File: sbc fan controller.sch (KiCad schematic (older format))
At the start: 26 parts, among them J1 Conn_01x13, J10 ISP-6, J2 Conn_01x02, J3 TEST_1P, J4 Conn_01x04, J5 Conn_01x04, J6 Conn_01x03, J7 TEST_1P, J8 TEST_2P, J9 Conn_Coaxial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

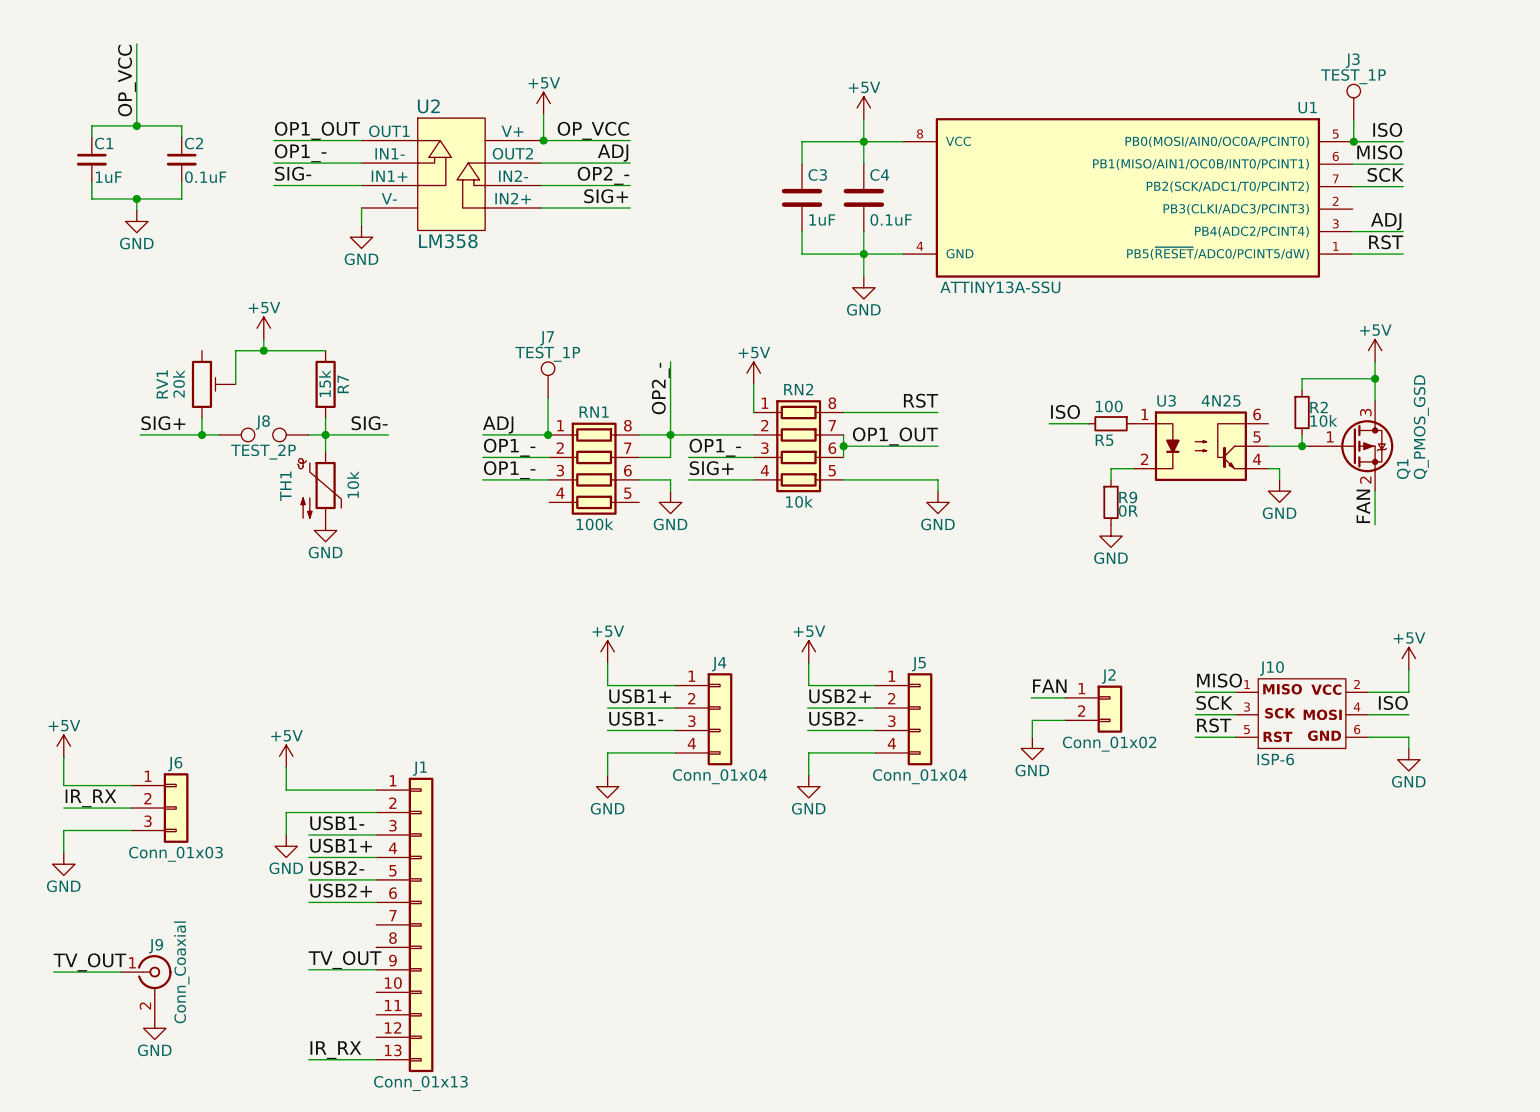
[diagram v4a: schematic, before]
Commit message: Simplified design, dropped amp; added isolated ground
After testing the dual amp circuit against a simple voltage divider, ADC yields enough resolution to discern heat levels in order to accommodate a look up table for fan speed. Isolated ground plane for switching area included to minimize EMF impact on integrated wifi.
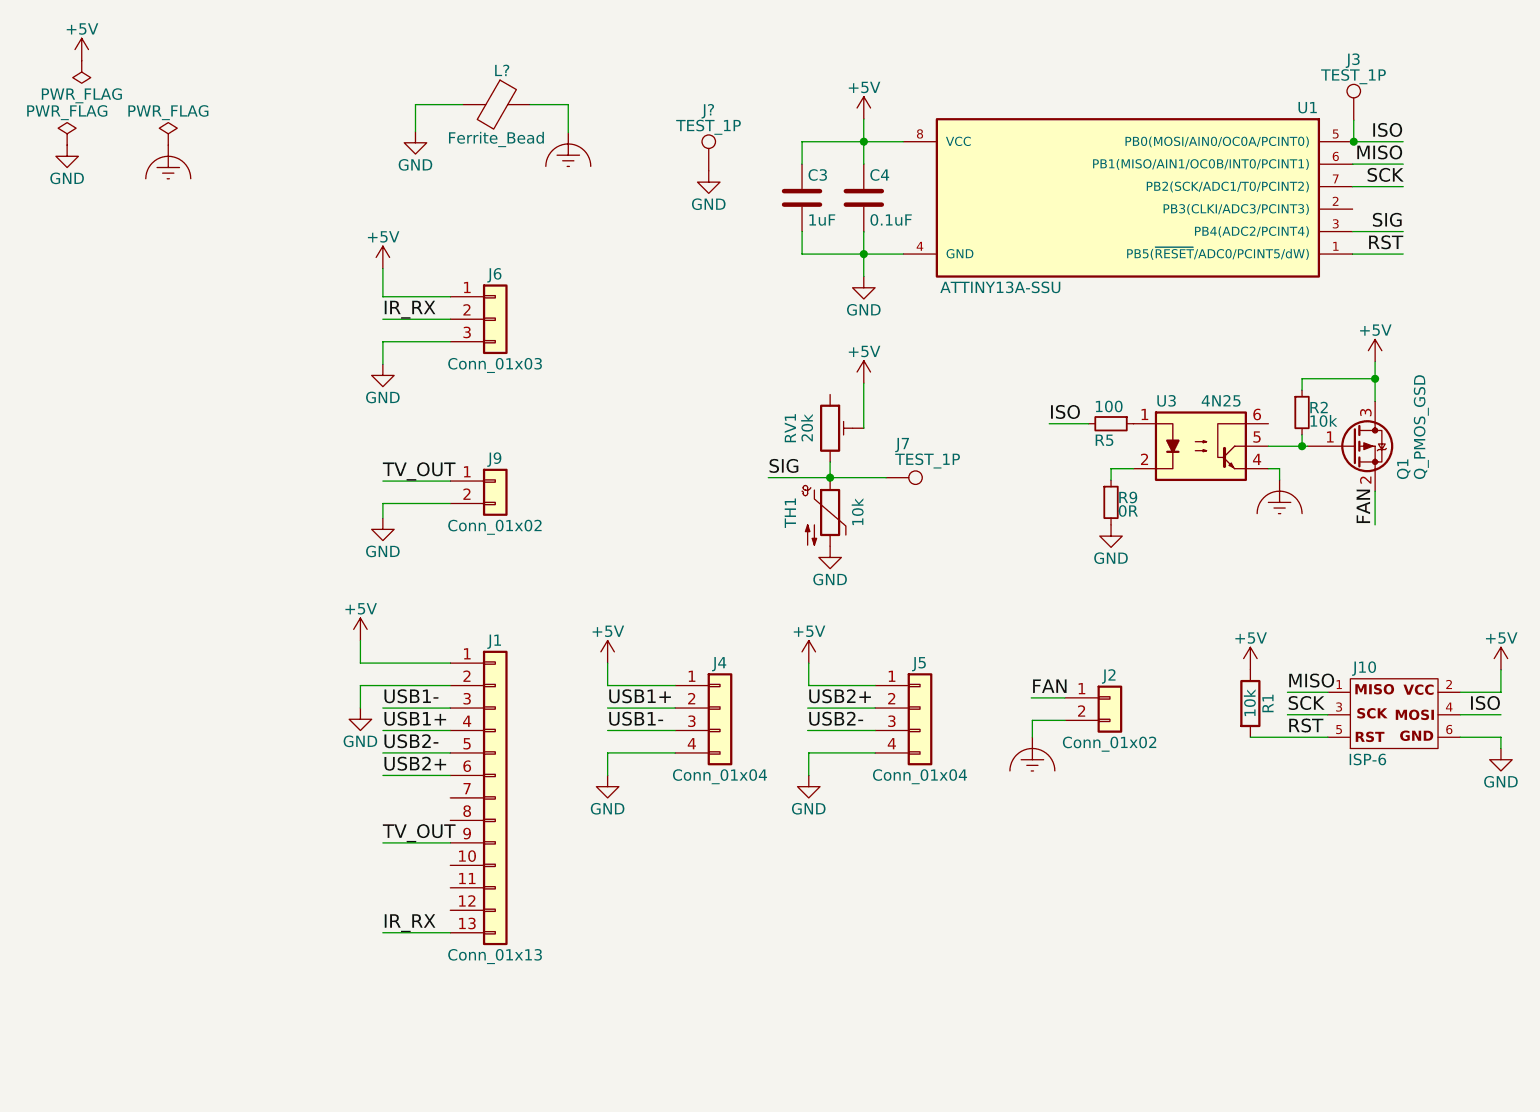
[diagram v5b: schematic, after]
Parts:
- removed C1: 1uF, Capacitors_SMD:C_0603, symbol C_Small
- removed C2: 0.1uF, Capacitors_SMD:C_0603, symbol C_Small
- removed J8: TEST_2P, node_nrf:Measurement_Point_Round-SMD-2-Pad_Small, symbol TEST_2P
- removed J9: Conn_Coaxial, rca:RCA1, symbol Conn_Coaxial
- removed R7: 15k, Resistors_SMD:R_0805, symbol R
- removed RN1: 100k, node_nrf:YC164J, symbol R_Pack04
- removed RN2: 10k, node_nrf:YC164J, symbol R_Pack04
- removed U2: LM358, Housings_SOIC:SOIC-8_3.9x4.9mm_Pitch1.27mm, symbol TL972
- added J9: Conn_01x02, Connectors_JST:JST_ZE_S02B-ZESK-2D_02x1.5mm_Angled, symbol Conn_01x02
- added J?: TEST_1P, symbol TEST_1P
- added L?: Ferrite_Bead, symbol Ferrite_Bead
- added R1: 10k, Resistors_SMD:R_0805, symbol R
- J4: footprint Connectors_JST:JST_SH_BM04B-SRSS-TB_04x1.00mm_Straight -> Connectors_JST:JST_ZE_S04B-ZESK-2D_04x1.5mm_Angled
- J5: footprint Connectors_JST:JST_SH_BM04B-SRSS-TB_04x1.00mm_Straight -> Connectors_JST:JST_ZE_SM04B-ZESS-TB_04x1.5mm_Angled
- J6: footprint Connectors_JST:JST_SH_BM03B-SRSS-TB_03x1.00mm_Straight -> Connectors_JST:JST_ZE_SM03B-ZESS-TB_03x1.5mm_Angled
- TH1: footprint Resistors_THT:R_Axial_DIN0204_L3.6mm_D1.6mm_P2.54mm_Vertical -> Connectors_JST:JST_ZE_SM02B-ZESS-TB_02x1.5mm_Angled
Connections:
- net ADJ is gone; now on net SIG: J7.1, U1.3 (PB4(ADC2/PCINT4))
- net SIG+ is gone; now on net SIG: RV1.3
- net +5V: now also R1.1
- net GND: now also J9.2 (Pin_2), J?.1, L?.2; no longer J2.2 (Pin_2), U3.4
- net RST: now also R1.2
- net TV_OUT: now also J9.1 (Pin_1)
- net SIG: now reaches TH1.1
- new net Earth_Clean: J2.2 (Pin_2), L?.1, U3.4
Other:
- moved on the sheet: J1, J10, J6, RV1, TH1

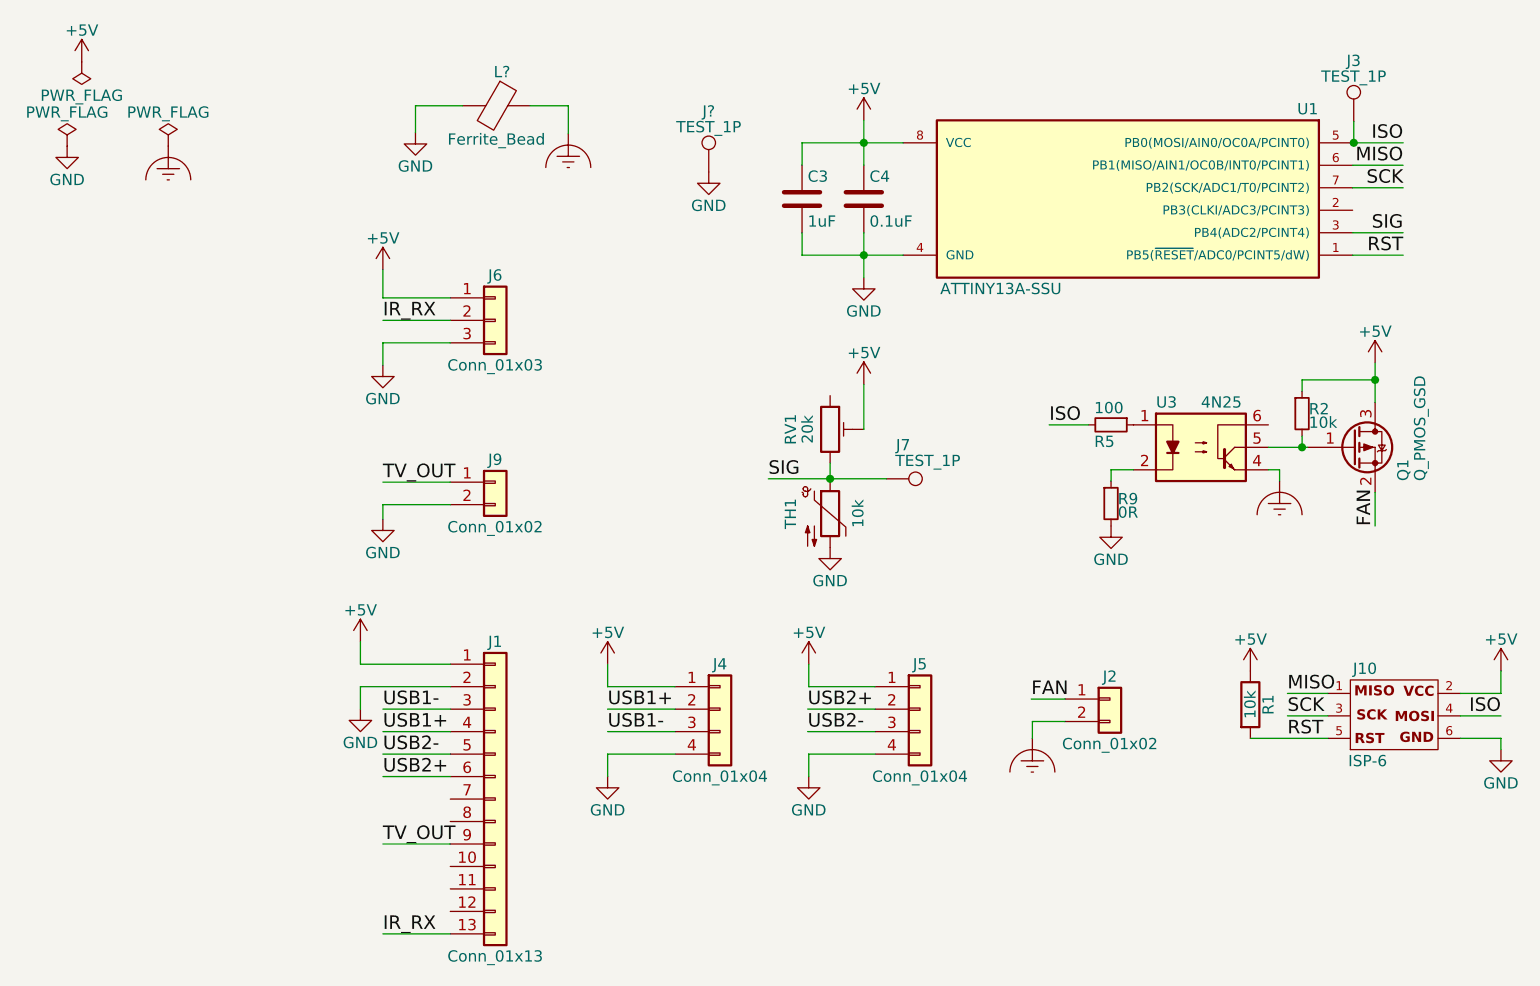
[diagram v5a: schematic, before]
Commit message: Final layout
Simplified layout and tested each footprint with a hard copy layout actual parts.
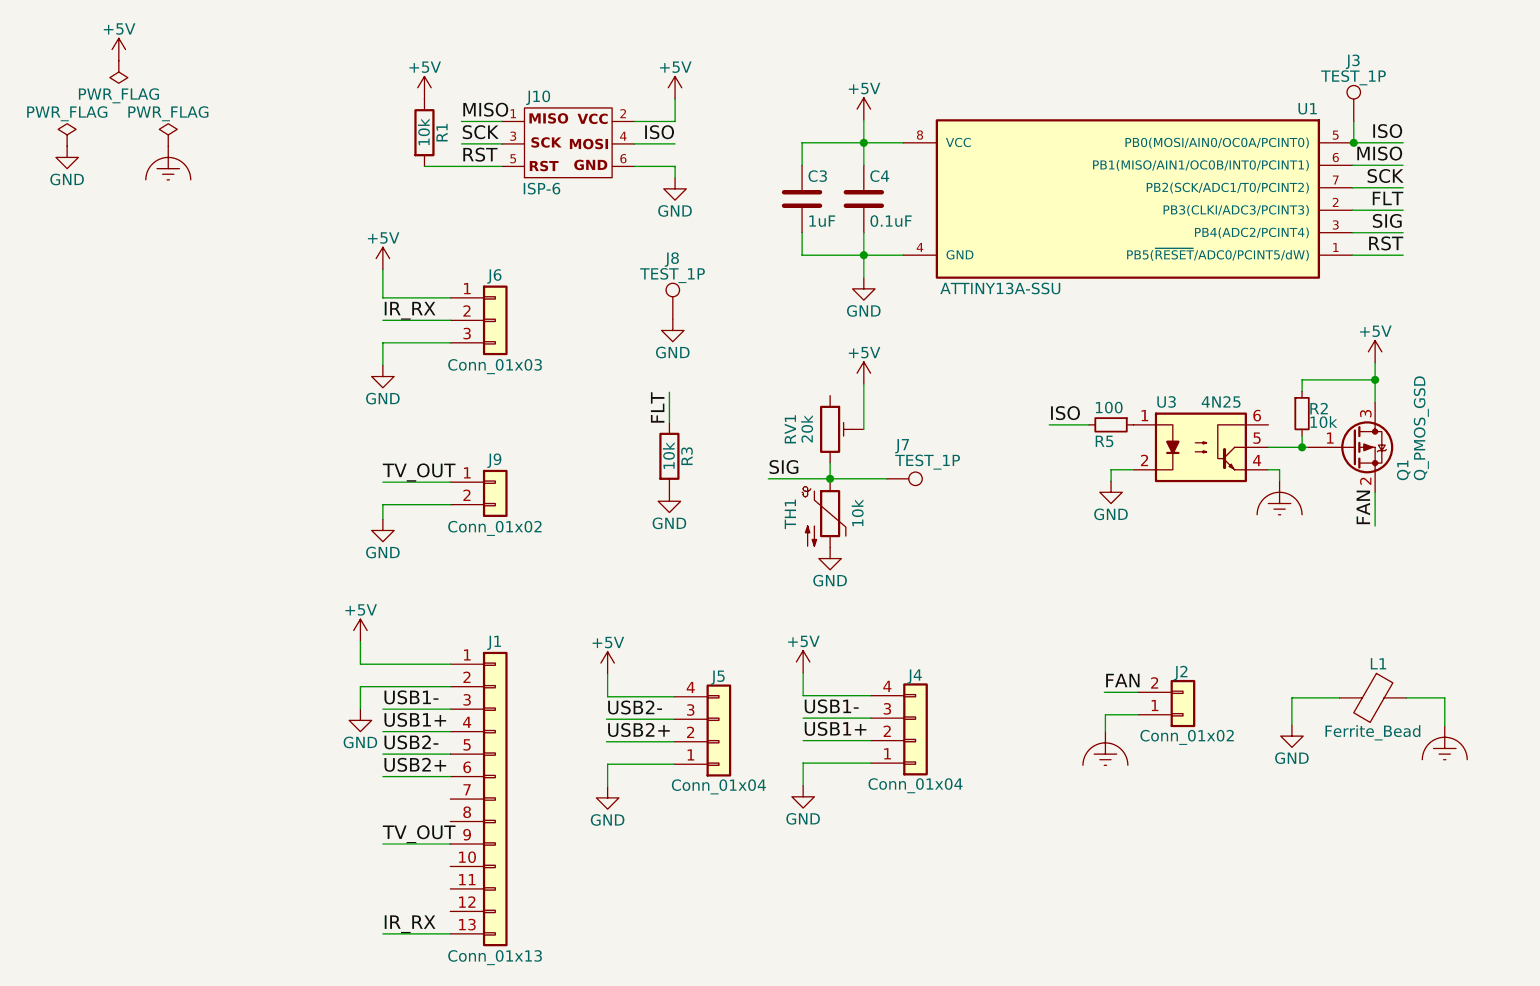
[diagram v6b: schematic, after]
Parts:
- removed R9: 0R, Resistors_SMD:R_0805, symbol R_Small
- added R3: 10k, Resistors_SMD:R_0805, symbol R
- J2: footprint Connectors_JST:JST_SH_BM02B-SRSS-TB_02x1.00mm_Straight -> JST_test_2:JST_ZH_SM02B-ZRSS-TB_1x02_P1.50mm_Horizontal
- J4: footprint Connectors_JST:JST_ZE_S04B-ZESK-2D_04x1.5mm_Angled -> JST_test_2:JST_ZH_SM04B-ZRSS-TB_1x04_P1.50mm_Horizontal
- J5: footprint Connectors_JST:JST_ZE_SM04B-ZESS-TB_04x1.5mm_Angled -> JST_test_2:JST_ZH_SM04B-ZRSS-TB_1x04_P1.50mm_Horizontal
- J6: footprint Connectors_JST:JST_ZE_SM03B-ZESS-TB_03x1.5mm_Angled -> JST_test_2:JST_ZH_SM03B-ZRSS-TB_1x03_P1.50mm_Horizontal
- J8: renamed from J?; footprint (none) -> Measurement_Points:Measurement_Point_Round-SMD-Pad_Small
- J9: footprint Connectors_JST:JST_ZE_S02B-ZESK-2D_02x1.5mm_Angled -> JST_test_2:JST_ZH_SM02B-ZRSS-TB_1x02_P1.50mm_Horizontal
- L1: renamed from L?; footprint (none) -> Resistors_SMD:R_0805
- TH1: footprint Connectors_JST:JST_ZE_SM02B-ZESS-TB_02x1.5mm_Angled -> JST_test_2:JST_ZH_SM02B-ZRSS-TB_1x02_P1.50mm_Horizontal
- U1: footprint Housings_SOIC:SO-8_5.3x6.2mm_Pitch1.27mm -> Housings_SOIC:SOIC-8_3.9x4.9mm_Pitch1.27mm
- U3: footprint SMD_Packages:SOIC-8-N -> 4n25_sop6:SO-6_4.4x3.6mm_Pitch1.27mm
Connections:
- net +5V: now also J4.4 (Pin_4), J5.4 (Pin_4); no longer J4.1 (Pin_1), J5.1 (Pin_1)
- net Earth_Clean: now also J2.1 (Pin_1); no longer J2.2 (Pin_2)
- net FAN: now also J2.2 (Pin_2); no longer J2.1 (Pin_1)
- net GND: now also J4.1 (Pin_1), J5.1 (Pin_1), U3.2, R3.2; no longer J4.4 (Pin_4), J5.4 (Pin_4)
- net FLT: now reaches U1.2 (PB3(CLKI/ADC3/PCINT3))
- net FLT: now also R3.1
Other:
- moved on the sheet: J10, J2, J4, J5, J8, L1, R1
